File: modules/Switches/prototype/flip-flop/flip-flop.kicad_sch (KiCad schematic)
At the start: 15 parts, among them J1 Conn_01x09, Q1 J109/J112, Q2 J109/J112, Q3 2N3906, SW1 SW_Push, U1 TL072

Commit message: Switches module - prototype wip
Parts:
- removed Q1, Q2: J109/J112, -lmp-misc:TO-92_Inline_Wide, symbol -lmp:Q_JFET_N_DSG
- removed Q3: 2N3906, -lmp-misc:TO-92_Inline_Wide, symbol -lmp:Q_PNP_2N3906
- removed R3: 1K, -lmp-stripboard:SB_Gen_2, symbol -lmp-synth:R_1K_Output
- removed R4: 240K, -lmp-stripboard:SB_Gen_2, symbol -lmp:R_1%_0W166
- removed R5, R7, R8: 10K, -lmp-stripboard:SB_Gen_2, symbol -lmp:R_1%_0W166
- removed R6: 10K, -lmp-misc:R_Axial_DIN0207_L6.3mm_D2.5mm_P7.62mm_Horizontal, symbol -lmp:R_1%_0W166
- removed U1: TL072, Package_DIP:DIP-8_W7.62mm, symbol -lmp-opamp:TL072
- added C2: 100N, -lmp-misc:C_Disc_D5.0mm_W2.5mm_P2.50mm, symbol -lmp:CC_100N
- added D1: LED, LED_THT:LED_D3.0mm_Clear, symbol -lmp-synth:LED_3mm_Red
- added R3: 10K, -lmp-misc:R_Axial_DIN0207_L6.3mm_D2.5mm_P7.62mm_Horizontal, symbol -lmp:R_1%_0W166
- added R4: 1K, -lmp-misc:R_Axial_DIN0207_L6.3mm_D2.5mm_P10.16mm_Horizontal, symbol -lmp-synth:R_1K_Output
- added U1: SN74HCS74, -lmp-breakout:Breakout_DIP-14_W15.24mm, symbol -lmp-IC-misc:SN74HCS74
- R1: value 100k -> 10K; footprint -lmp-stripboard:SB_Gen_1 -> -lmp-misc:R_Axial_DIN0207_L6.3mm_D2.5mm_P7.62mm_Horizontal
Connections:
- net +5V: now also R1.1, C2.1, U1.1 (~{R}), U1.10 (~{S}), U1.11 (C), U1.12 (D), U1.13 (~{R}), U1.14 (VDD)
- net GND: now also R2.2, D1.1 (K), U1.7 (VSS); no longer R1.1
- net IN-OUT-1: no longer R1.2
- net BUS-CV: now reaches J1.8 (Pin_8)
- net BUS-GATE: now reaches J1.9 (Pin_9)
- net at SW1.4: now also R2.1, R3.1
- net at C1.1: now also R1.2, U1.4 (~{S})
- new net: C2.2, R3.2, U1.3 (C)
- new net: U1.2 (D), U1.6 (~{Q})
- new net: R4.1, U1.5 (Q)
- new net: D1.2 (A), R4.2
- no-connect marks 7 -> 11
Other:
- title: JFET Switch Prototype -> Flip-Flop Test

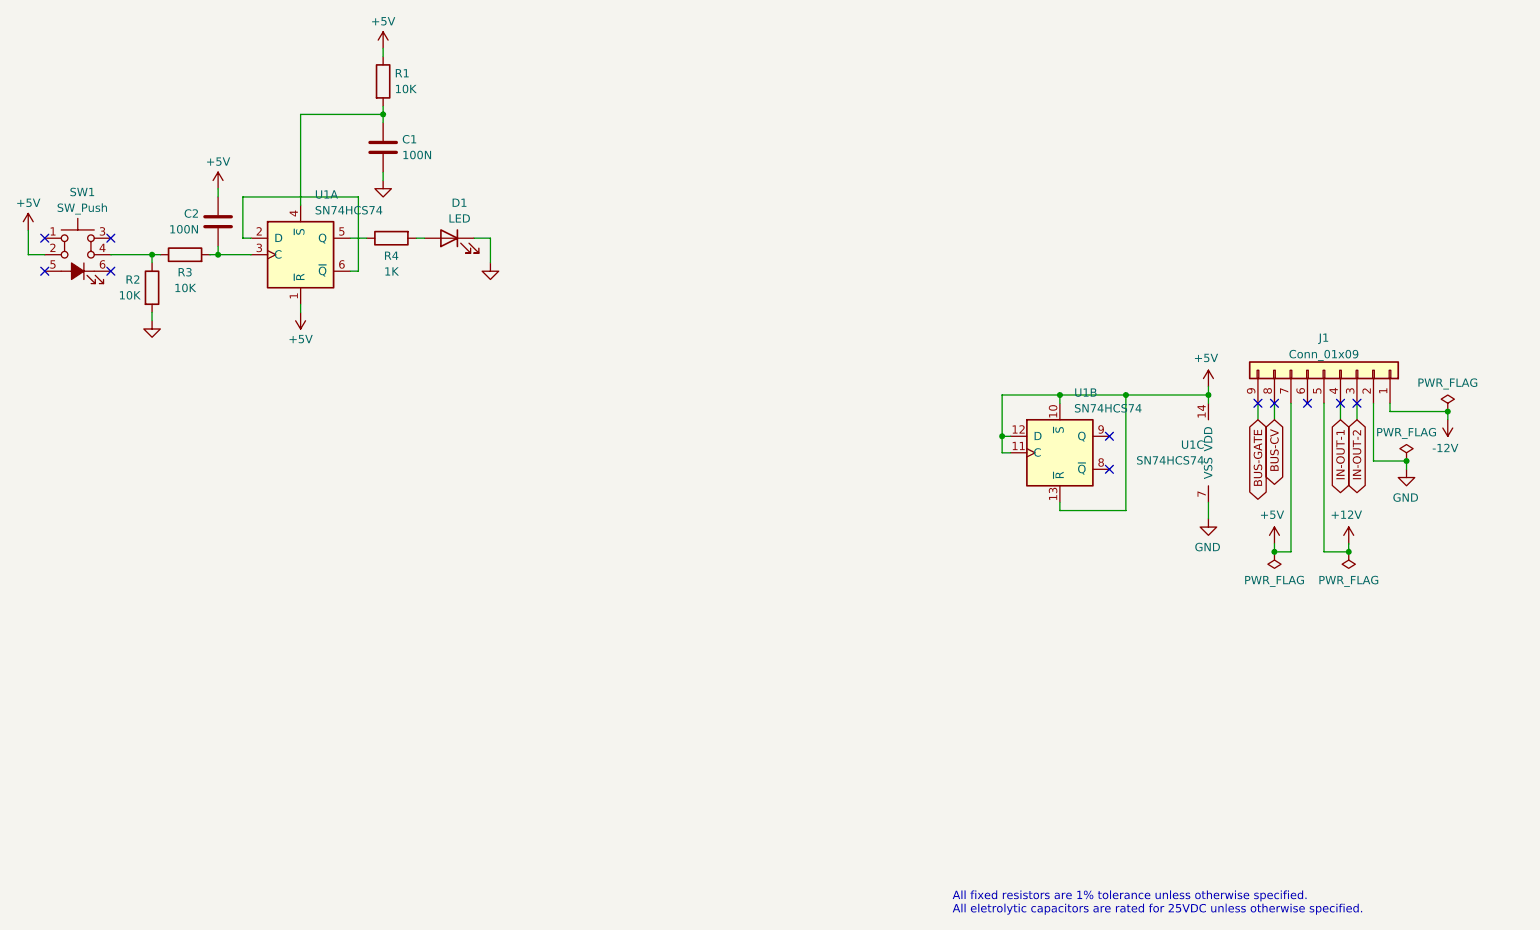
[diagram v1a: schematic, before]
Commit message: Switches module - flipflop test
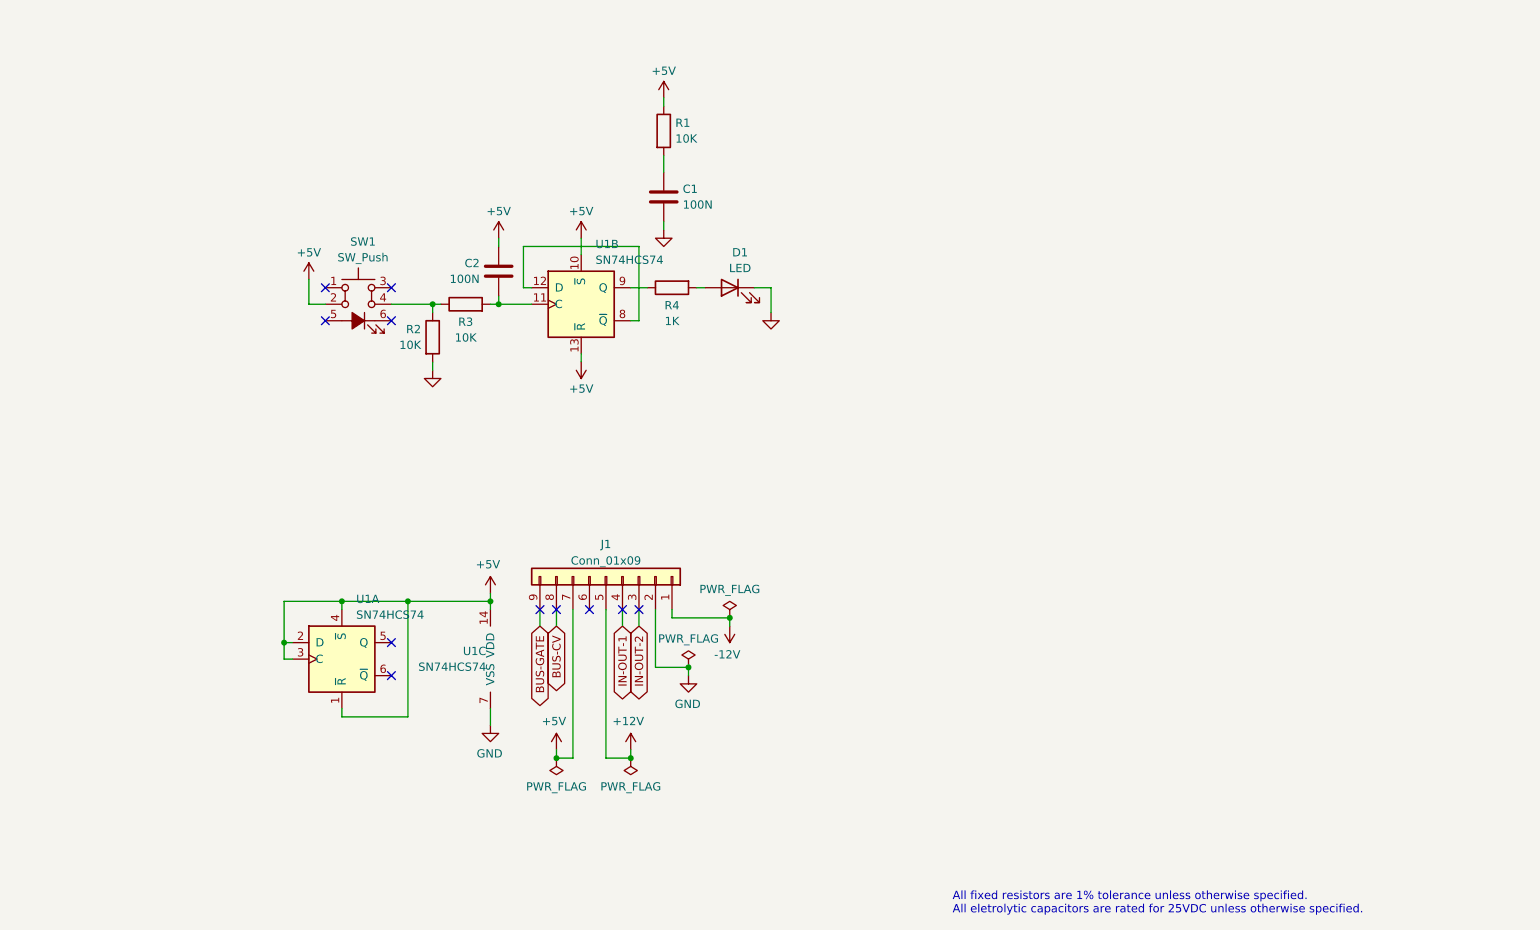
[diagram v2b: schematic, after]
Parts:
- C2: footprint -lmp-misc:C_Disc_D5.0mm_W2.5mm_P2.50mm -> -lmp-stripboard:SB_Gen_2
- R4: footprint -lmp-misc:R_Axial_DIN0207_L6.3mm_D2.5mm_P10.16mm_Horizontal -> -lmp-stripboard:SB_Gen_6
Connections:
- net +5V: now also U1.2 (D), U1.3 (C), U1.4 (~{S}); no longer U1.11 (C), U1.12 (D)
- net at C2.2, R3.2: now also U1.11 (C); no longer U1.3 (C)
- net at U1.6 (~{Q}): no longer U1.2 (D)
- net at C1.1, R1.2: no longer U1.4 (~{S})
- net at U1.5 (Q): no longer R4.1
- net at U1.8 (~{Q}): now also U1.12 (D)
- net at U1.9 (Q): now also R4.1
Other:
- moved on the sheet: C1, C2, D1, J1, R1, R2, R3, R4, SW1, U1A, U1B, U1C

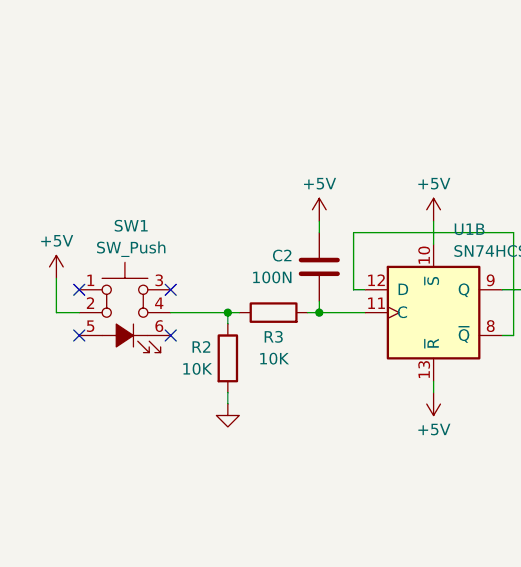
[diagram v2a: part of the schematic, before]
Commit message: Switches module - flipflop testing - wip
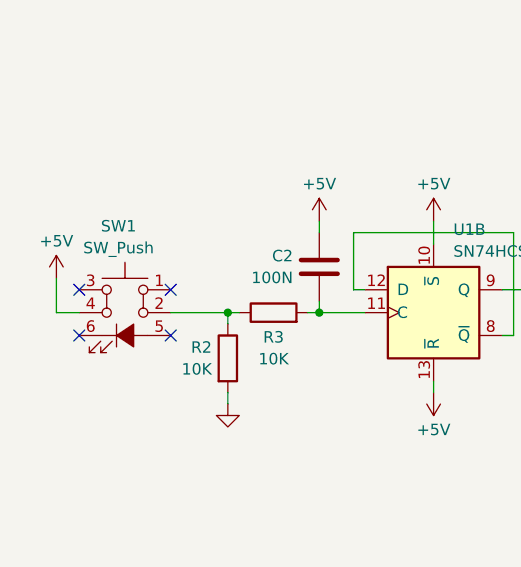
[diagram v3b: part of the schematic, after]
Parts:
- R2: footprint -lmp-misc:R_Axial_DIN0207_L6.3mm_D2.5mm_P7.62mm_Horizontal -> -lmp-stripboard:SB_Gen_1
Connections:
- net +5V: now also SW1.4; no longer SW1.2
- net at R2.1, R3.1: now also SW1.2; no longer SW1.4
